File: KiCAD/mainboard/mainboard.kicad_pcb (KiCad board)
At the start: 2 copper layers, 4 parts, among them IC1 DLPC1438ZEZ, IC2 DLPA2005ERSLT, J1 AXT550124

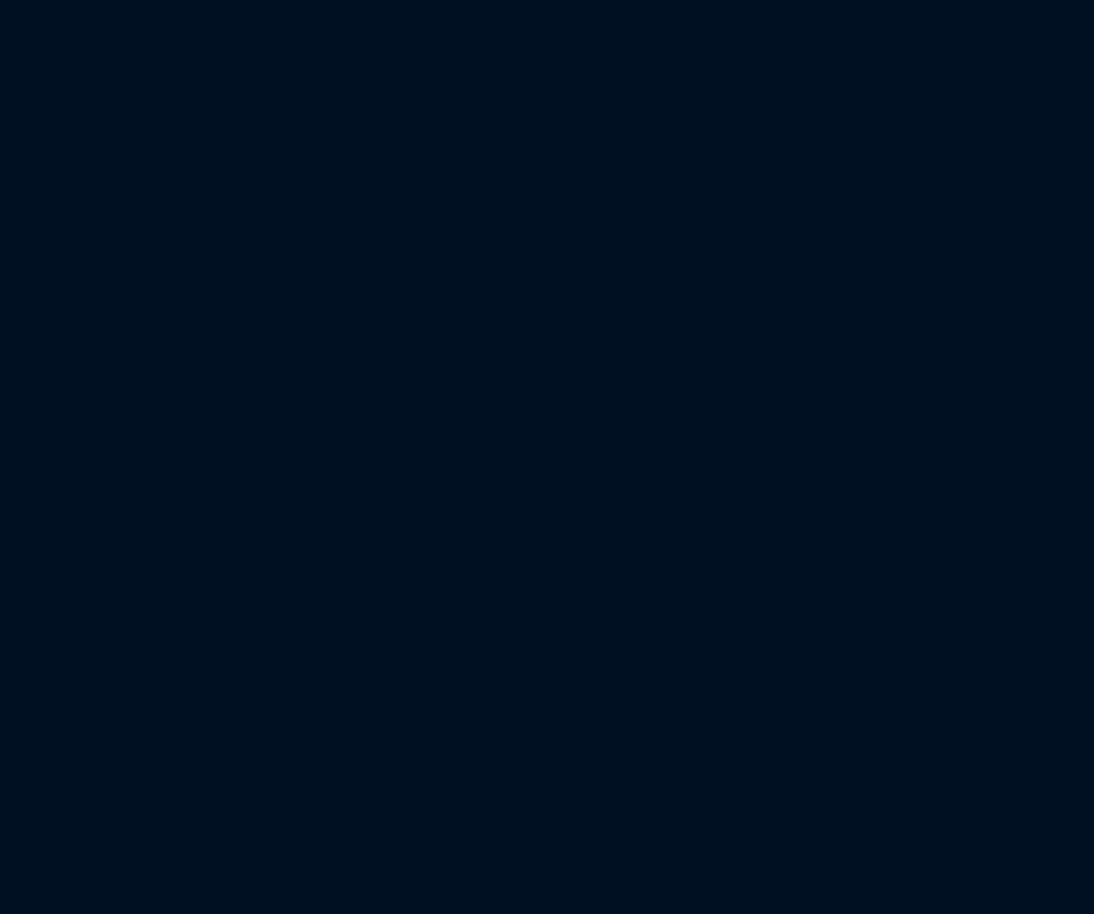
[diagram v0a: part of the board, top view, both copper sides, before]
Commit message: WIP dmd interface; made assembly for DMD, started new board for DMD interconnect
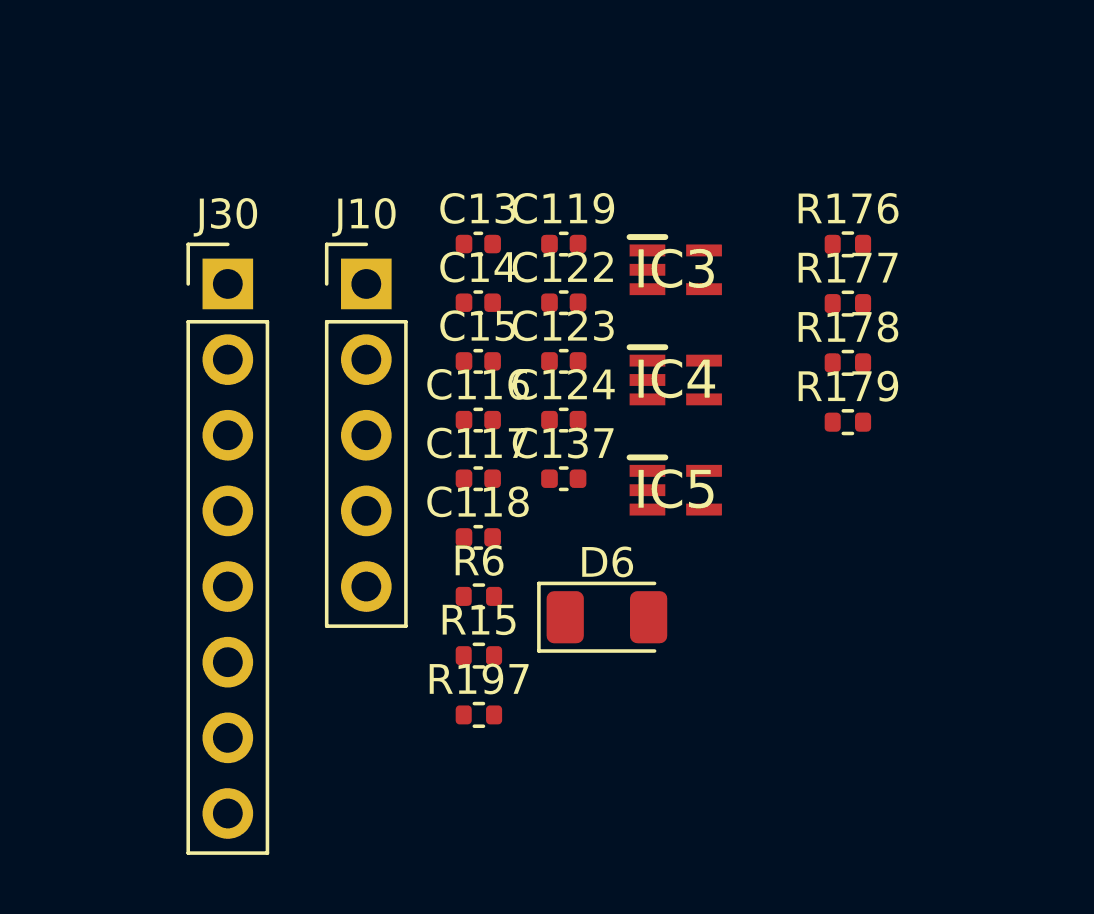
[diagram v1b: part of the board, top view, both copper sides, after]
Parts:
- added C116: 100n, Capacitor_SMD:C_0402_1005Metric, F.Cu at (144.9, 105.4)
- added C117: 220n, Capacitor_SMD:C_0402_1005Metric, F.Cu at (144.9, 107.4)
- added C118: 220n, Capacitor_SMD:C_0402_1005Metric, F.Cu at (144.9, 109.4)
- added C119: 220n, Capacitor_SMD:C_0402_1005Metric, F.Cu at (147.8, 99.5)
- added C122: 100n, Capacitor_SMD:C_0402_1005Metric, F.Cu at (147.8, 101.5)
- added C123: 100n, Capacitor_SMD:C_0402_1005Metric, F.Cu at (147.8, 103.5)
- added C124: 100n, Capacitor_SMD:C_0402_1005Metric, F.Cu at (147.8, 105.4)
- added C13: 100n, Capacitor_SMD:C_0402_1005Metric, F.Cu at (144.9, 99.5)
- added C137: 100n, Capacitor_SMD:C_0402_1005Metric, F.Cu at (147.8, 107.4)
- added C14: 100n, Capacitor_SMD:C_0402_1005Metric, F.Cu at (144.9, 101.5)
- added C15: 100n, Capacitor_SMD:C_0402_1005Metric, F.Cu at (144.9, 103.5)
- added D6: LED, LED_SMD:LED_1206_3216Metric, F.Cu at (149.2, 112.0)
- added IC3: SN74AUP1G06DCKR, tp_library:SOT65P210X110-5N, F.Cu at (151.5, 100.4)
- added IC4: SN74AUP1G07DCKR, tp_library:SOT65P210X110-5N, F.Cu at (151.5, 104.1)
- added IC5: SN74AUP1G07DCKR, tp_library:SOT65P210X110-5N, F.Cu at (151.5, 107.8)
- added J10: Conn_01x05_Pin, Connector_PinHeader_2.54mm:PinHeader_1x05_P2.54mm_Vertical, F.Cu at (141.1, 100.9)
- added J30: Conn_01x08_Pin, Connector_PinHeader_2.54mm:PinHeader_1x08_P2.54mm_Vertical, F.Cu at (136.5, 100.9)
- added R15: 10k, Resistor_SMD:R_0402_1005Metric, F.Cu at (144.9, 113.3)
- added R176: 100k, Resistor_SMD:R_0402_1005Metric, F.Cu at (157.3, 99.5)
- added R177: 100k, Resistor_SMD:R_0402_1005Metric, F.Cu at (157.3, 101.5)
- added R178: 100k, Resistor_SMD:R_0402_1005Metric, F.Cu at (157.3, 103.5)
- added R179: 100k, Resistor_SMD:R_0402_1005Metric, F.Cu at (157.3, 105.5)
- added R197: 10k, Resistor_SMD:R_0402_1005Metric, F.Cu at (144.9, 115.3)
- added R6: 150, Resistor_SMD:R_0402_1005Metric, F.Cu at (144.9, 111.3)
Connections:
- IC1 pad A1: unconnected-(IC1-DMD_LS_C_LK-PadA1) -> /DLPC1438_Interface/LS_CLK
- IC1 pad A10: unconnected-(IC1-DMD_HS_W_DATAB_P-PadA10) -> /DLPC1438_Interface/DMD_HS_WDATAB_P
- IC1 pad A11: unconnected-(IC1-DMD_HS_W_DATAA_P-PadA11) -> /DLPC1438_Interface/DMD_HS_WDATAA_P
- IC1 pad A2: unconnected-(IC1-DMD_LS_W_DATA-PadA2) -> /DLPC1438_Interface/LS_WDATA
- IC1 pad A3: unconnected-(IC1-DMD_HS_W_DATAH_P-PadA3) -> /DLPC1438_Interface/DMD_HS_WDATAH_P
- IC1 pad A4: unconnected-(IC1-DMD_HS_W_DATAG_P-PadA4) -> /DLPC1438_Interface/DMD_HS_WDATAG_P
- IC1 pad A5: unconnected-(IC1-DMD_HS_W_DATAF_P-PadA5) -> /DLPC1438_Interface/DMD_HS_WDATAF_P
- IC1 pad A6: unconnected-(IC1-DMD_HS_W_DATAE_P-PadA6) -> /DLPC1438_Interface/DMD_HS_WDATAE_P
- IC1 pad A7: unconnected-(IC1-DMD_HS_CLK__P-PadA7) -> /DLPC1438_Interface/DMD_HS_CLK_P
- IC1 pad A8: unconnected-(IC1-DMD_HS_W_DATAD_P-PadA8) -> /DLPC1438_Interface/DMD_HS_WDATAD_P
- IC1 pad A9: unconnected-(IC1-DMD_HS_W_DATAC_P-PadA9) -> /DLPC1438_Interface/DMD_HS_WDATAC_P
- IC1 pad B1: unconnected-(IC1-DMD_DEN__ARSTZ-PadB1) -> /DLPC1438_Interface/DMD_DEN_ARSTZ
- IC1 pad B10: unconnected-(IC1-DMD_HS_W_DATAB_N-PadB10) -> /DLPC1438_Interface/DMD_HS_WDATAB_N
- IC1 pad B11: unconnected-(IC1-DMD_HS_W_DATAA_N-PadB11) -> /DLPC1438_Interface/DMD_HS_WDATAA_N
- IC1 pad B2: unconnected-(IC1-DMD_LS_R_DATA-PadB2) -> /DLPC1438_Interface/DMD_LS_RDATA
- IC1 pad B3: unconnected-(IC1-DMD_HS_W_DATAH_N-PadB3) -> /DLPC1438_Interface/DMD_HS_WDATAH_N
- IC1 pad B4: unconnected-(IC1-DMD_HS_W_DATAG_N-PadB4) -> /DLPC1438_Interface/DMD_HS_WDATAG_N
- IC1 pad B5: unconnected-(IC1-DMD_HS_W_DATAF_N-PadB5) -> /DLPC1438_Interface/DMD_HS_WDATAF_N
- IC1 pad B6: unconnected-(IC1-DMD_HS_W_DATAE_N-PadB6) -> /DLPC1438_Interface/DMD_HS_WDATAE_N
- IC1 pad B7: unconnected-(IC1-DMD_HS_CLK__N-PadB7) -> /DLPC1438_Interface/DMD_HS_CLK_N
- IC1 pad B8: unconnected-(IC1-DMD_HS_W_DATAD_N-PadB8) -> /DLPC1438_Interface/DMD_HS_WDATAD_N
- IC1 pad B9: unconnected-(IC1-DMD_HS_W_DATAC_N-PadB9) -> /DLPC1438_Interface/DMD_HS_WDATAC_N
- IC1 pad C14: unconnected-(IC1-GPIO_00-PadC14) -> SPI1_MISO
- IC1 pad C15: unconnected-(IC1-GPIO_01-PadC15) -> /DLPC1438_Interface/GPIO_1
- IC1 pad D14: unconnected-(IC1-GPIO_02-PadD14) -> /DLPC1438_Interface/GPIO_2
- IC1 pad D15: unconnected-(IC1-GPIO_03-PadD15) -> /DLPC1438_Interface/GPIO_3
- IC1 pad E14: unconnected-(IC1-GPIO_04-PadE14) -> GPIO_4
- IC1 pad E15: unconnected-(IC1-GPIO_05-PadE15) -> GPIO_5
- IC1 pad F14: unconnected-(IC1-GPIO_06-PadF14) -> GPIO_6
- IC1 pad F15: unconnected-(IC1-GPIO_07-PadF15) -> /DLPC1438_Interface/ACT_SYNC
- IC1 pad G14: unconnected-(IC1-GPIO_08-PadG14) -> /DLPC1438_Interface/PROJ_ON
- IC1 pad G15: unconnected-(IC1-GPIO_09-PadG15) -> GPIO_9
- IC1 pad H14: unconnected-(IC1-GPIO_10-PadH14) -> /DLPC1438_Interface/RC_CHARGE
- IC1 pad H15: unconnected-(IC1-GPIO_11-PadH15) -> /DLPC1438_Interface/THERM_PWR
- IC1 pad J14: unconnected-(IC1-GPIO_12-PadJ14) -> GPIO_12
- IC1 pad K14: unconnected-(IC1-GPIO_14-PadK14) -> /DLPC1438_Interface/FPGA_RDY
- IC1 pad K15: unconnected-(IC1-GPIO_15-PadK15) -> GPIO_15
- IC1 pad L14: unconnected-(IC1-GPIO_16-PadL14) -> GPIO_16
- IC1 pad L15: unconnected-(IC1-GPIO_17-PadL15) -> GPIO_17
- IC1 pad M14: unconnected-(IC1-GPIO_18-PadM14) -> GPIO_18
- IC1 pad M15: unconnected-(IC1-GPIO_19-PadM15) -> GPIO_19
- J1 pad 1: unconnected-(J1-Pad1) -> P1P8V_DLPC
- J1 pad 10: unconnected-(J1-19-Pad10) -> /DLPC1438_Interface/DMD_HS_WDATAG_P
- J1 pad 11: unconnected-(J1-Pad11) -> /DLPC1438_Interface/DMD_HS_WDATAG_N
- J1 pad 12: unconnected-(J1-Pad12) -> GND
- J1 pad 13: unconnected-(J1-Pad13) -> /DLPC1438_Interface/DMD_HS_CLK_P
- J1 pad 14: unconnected-(J1-Pad14) -> /DLPC1438_Interface/DMD_HS_CLK_N
- J1 pad 15: unconnected-(J1-Pad15) -> GND
- J1 pad 16: unconnected-(J1-Pad16) -> /DLPC1438_Interface/DMD_HS_WDATAB_P
- J1 pad 17: unconnected-(J1-Pad17) -> /DLPC1438_Interface/DMD_HS_WDATAB_N
- J1 pad 18: unconnected-(J1-Pad18) -> /DLPC1438_Interface/DMD_HS_WDATAA_P
- J1 pad 19: unconnected-(J1-Pad19) -> /DLPC1438_Interface/DMD_HS_WDATAA_N
- J1 pad 2: unconnected-(J1-Pad2) -> GND
- J1 pad 20: unconnected-(J1-Pad20) -> GND
- J1 pad 21: unconnected-(J1-Pad21) -> GND
- J1 pad 22: unconnected-(J1-Pad22) -> GND
- J1 pad 25: unconnected-(J1-49-Pad25) -> GND
- J1 pad 26: unconnected-(J1-Pad26) -> GND
- J1 pad 3: unconnected-(J1-Pad3) -> /DLPC1438_Interface/DMD_LS_RDATA
- J1 pad 30: unconnected-(J1-Pad30) -> GND
- J1 pad 31: unconnected-(J1-Pad31) -> GND
- J1 pad 32: unconnected-(J1-Pad32) -> /DLPC1438_Interface/DMD_HS_WDATAC_N
- J1 pad 33: unconnected-(J1-Pad33) -> /DLPC1438_Interface/DMD_HS_WDATAC_P
- J1 pad 34: unconnected-(J1-Pad34) -> /DLPC1438_Interface/DMD_HS_WDATAD_N
- J1 pad 35: unconnected-(J1-Pad35) -> /DLPC1438_Interface/DMD_HS_WDATAD_P
- J1 pad 36: unconnected-(J1-Pad36) -> GND
- J1 pad 37: unconnected-(J1-Pad37) -> P1P8V_DLPC
- J1 pad 38: unconnected-(J1-Pad38) -> P1P8V_DLPC
- J1 pad 39: unconnected-(J1-Pad39) -> GND
- J1 pad 4: unconnected-(J1-Pad4) -> /DLPC1438_Interface/DMD_DEN_ARSTZ
- J1 pad 40: unconnected-(J1-Pad40) -> /DLPC1438_Interface/DMD_HS_WDATAE_N
- J1 pad 41: unconnected-(J1-Pad41) -> /DLPC1438_Interface/DMD_HS_WDATAE_P
- J1 pad 42: unconnected-(J1-Pad42) -> /DLPC1438_Interface/DMD_HS_WDATAF_N
- J1 pad 43: unconnected-(J1-Pad43) -> /DLPC1438_Interface/DMD_HS_WDATAF_P
- J1 pad 44: unconnected-(J1-Pad44) -> GND
- J1 pad 45: unconnected-(J1-Pad45) -> /DMD_Interface/VRST
- J1 pad 46: unconnected-(J1-Pad46) -> /DMD_Interface/VBIAS
- J1 pad 47: unconnected-(J1-Pad47) -> /DMD_Interface/VOFS
- J1 pad 48: unconnected-(J1-Pad48) -> GND
- J1 pad 49: unconnected-(J1-Pad49) -> GND
- J1 pad 5: unconnected-(J1-Pad5) -> /DLPC1438_Interface/LS_WDATA
- J1 pad 50: unconnected-(J1-Pad50) -> P1P8V_DLPC
- J1 pad 51: unconnected-(J1-MP1-Pad51) -> GND
- J1 pad 52: unconnected-(J1-MP2-Pad52) -> GND
- J1 pad 53: unconnected-(J1-MP3-Pad53) -> GND
- J1 pad 54: unconnected-(J1-MP4-Pad54) -> GND
- J1 pad 6: unconnected-(J1-Pad6) -> /DLPC1438_Interface/LS_CLK
- J1 pad 7: unconnected-(J1-Pad7) -> GND
- J1 pad 8: unconnected-(J1-Pad8) -> /DLPC1438_Interface/DMD_HS_WDATAH_P
- J1 pad 9: unconnected-(J1-Pad9) -> /DLPC1438_Interface/DMD_HS_WDATAH_N

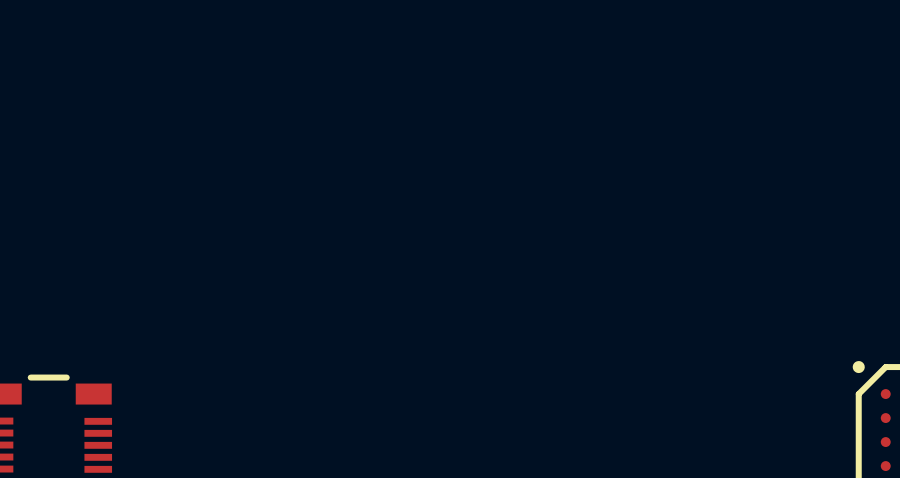
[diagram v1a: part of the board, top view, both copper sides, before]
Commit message: added libraries and symbols and step for ferrite beads and D7 LED
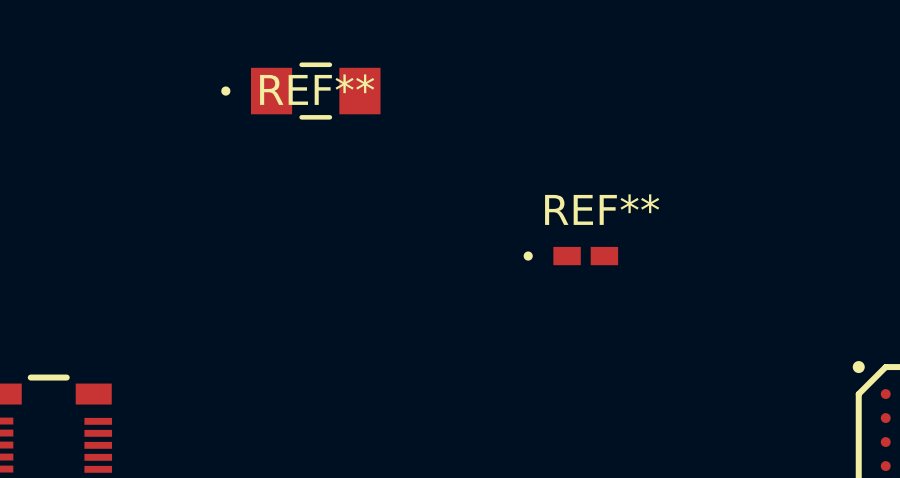
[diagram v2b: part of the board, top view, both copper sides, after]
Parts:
- added REF**: BLM15P_FBD, tp_library:BLM15P_FBD-M, F.Cu at (138.0, 52.5)
- added REF**: LED_SML-LX1206SIC-TR_LUM, tp_library:LED_SML-LX1206SIC-TR_LUM-M, F.Cu at (129.0, 47.0)

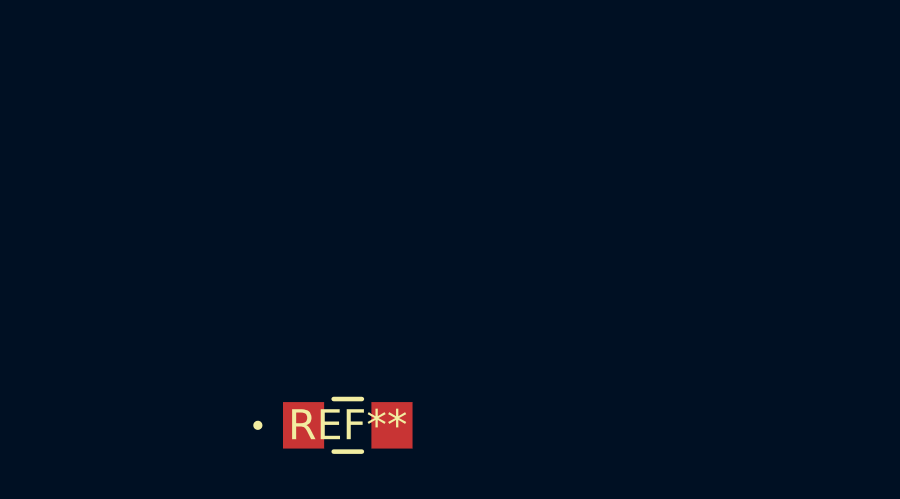
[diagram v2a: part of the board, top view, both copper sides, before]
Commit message: added sym mod and step for resistors but package 0805
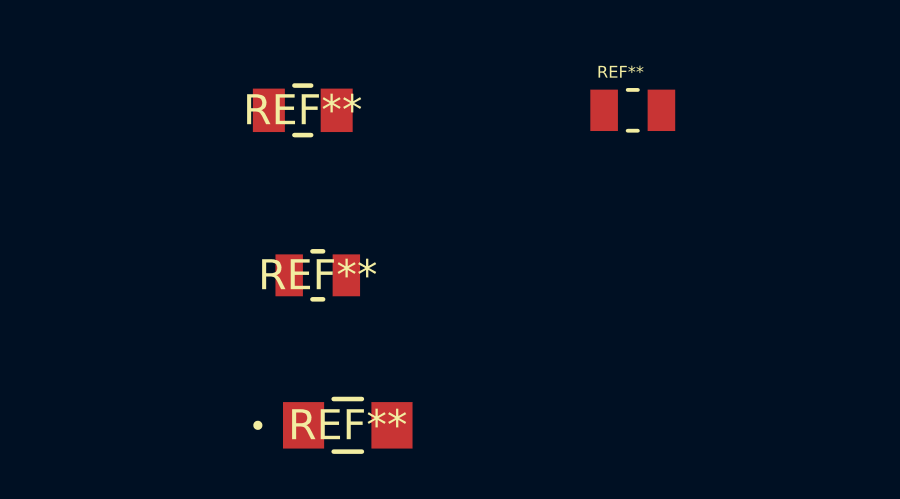
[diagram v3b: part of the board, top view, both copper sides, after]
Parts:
- added REF**: RESC2012X60N, tp_library:RESC2012X60N, F.Cu at (138.5, 36.5)
- added REF**: RES_CRCW_0805, tp_library:RES_CRCW_0805-M, F.Cu at (127.5, 36.5)
- added REF**: STA_RMCF0805_STP, tp_library:STA_RMCF0805_STP-M, F.Cu at (128.0, 42.0)

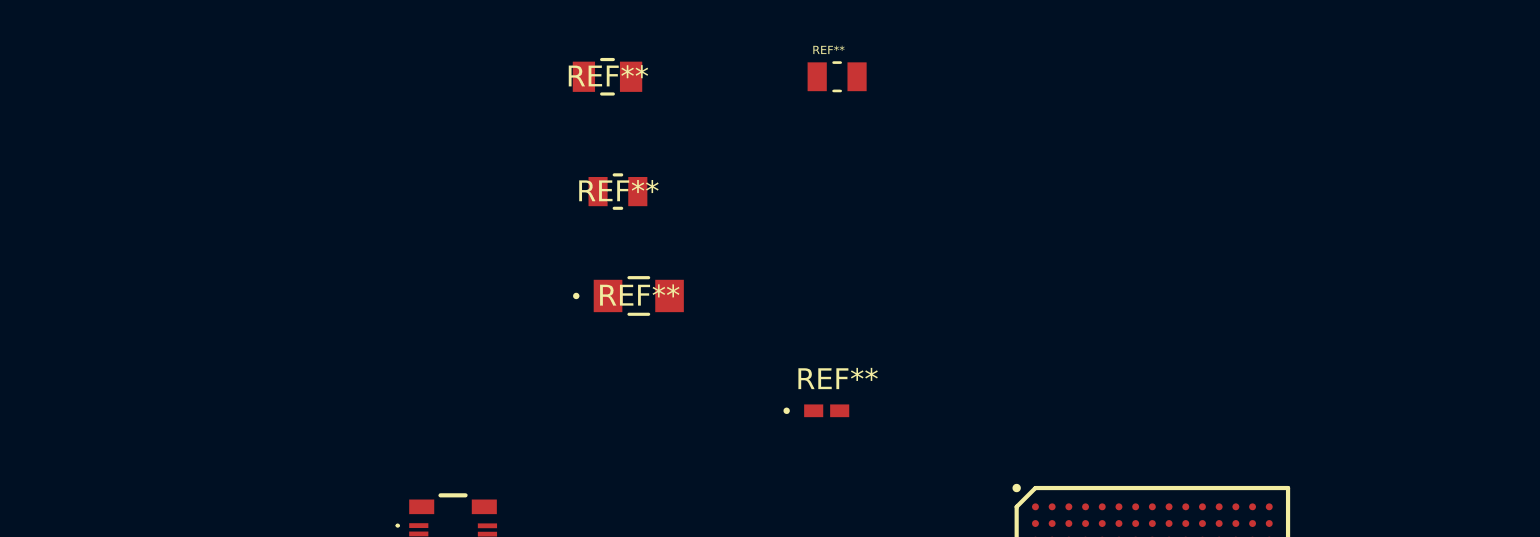
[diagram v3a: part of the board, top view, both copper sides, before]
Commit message: replaced with 0805 all passives in DLPC
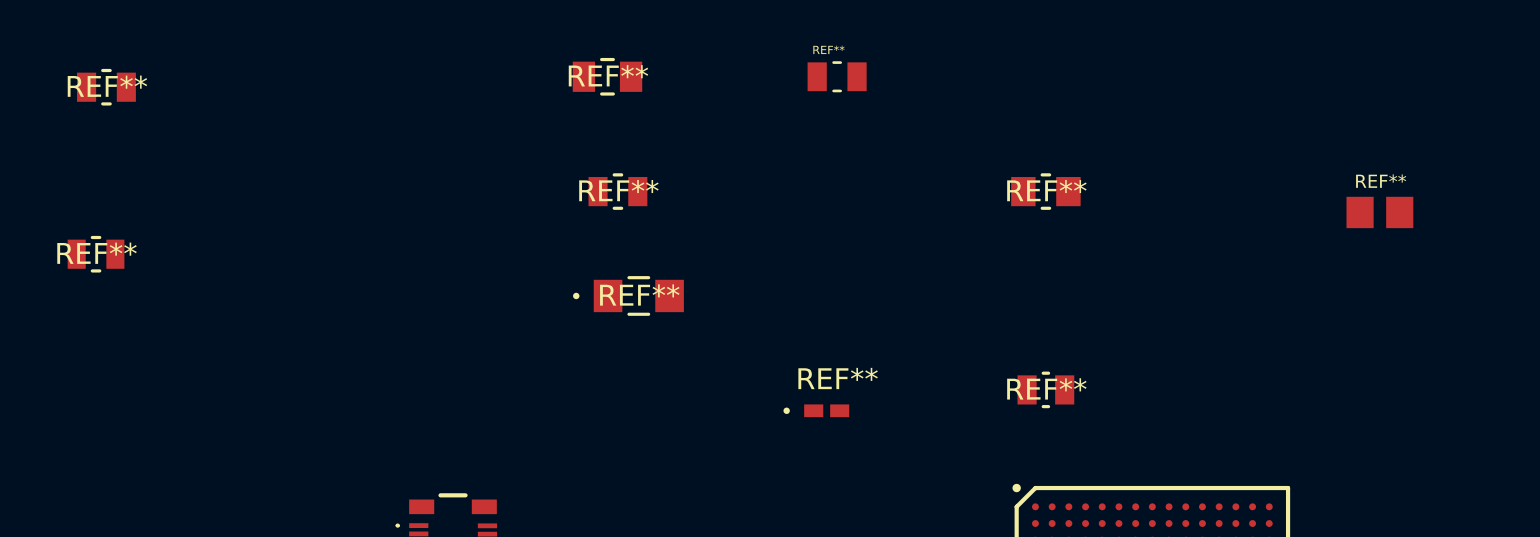
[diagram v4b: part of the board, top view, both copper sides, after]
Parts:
- added REF**: RES_R-070RL_VIS, tp_library:RES_R-070RL_VIS-M, F.Cu at (103.0, 45.0)
- added REF**: CAPC2012X70, tp_library:CAPC2012X70, F.Cu at (164.5, 43.0)
- added REF**: RES_ERJP06_PAN, tp_library:RES_ERJP06_PAN-M, F.Cu at (103.5, 37.0)
- added REF**: RES_RM10_CCE, tp_library:RES_RM10_CCE-M, F.Cu at (148.5, 51.5)
- added REF**: RES_RMCF0805_STP, tp_library:RES_RMCF0805_STP-M, F.Cu at (148.5, 42.0)
